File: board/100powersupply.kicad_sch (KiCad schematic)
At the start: 10 parts, among them J103 Conn_02x02_Counter_Clockwise, U101 TLS850C2TEV33

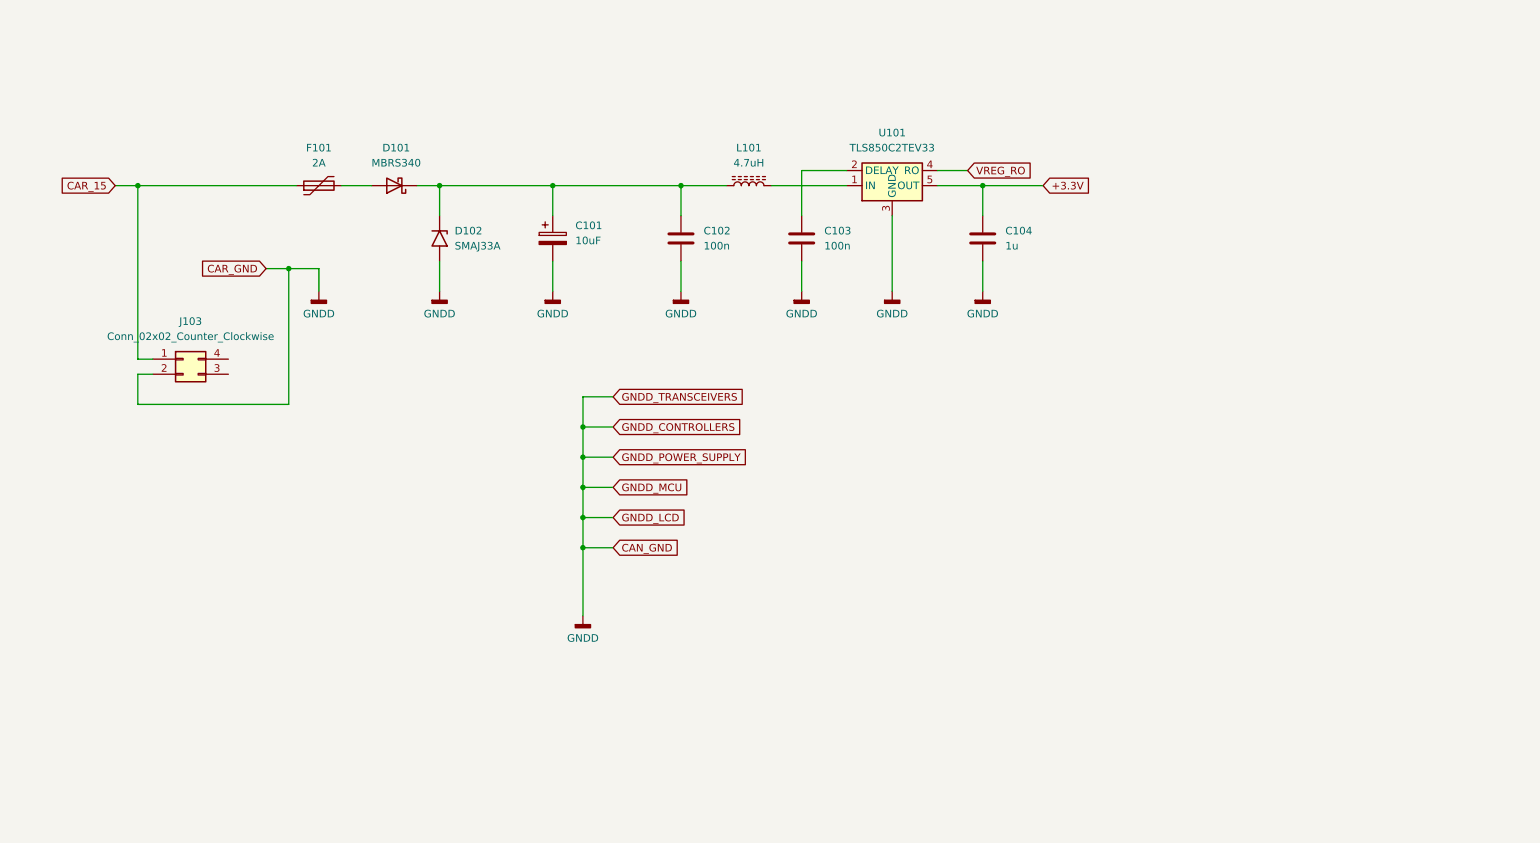
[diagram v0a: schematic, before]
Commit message: Added stl and skp files for 3D printing, changed ground planes and net names, exported schematics as pdf
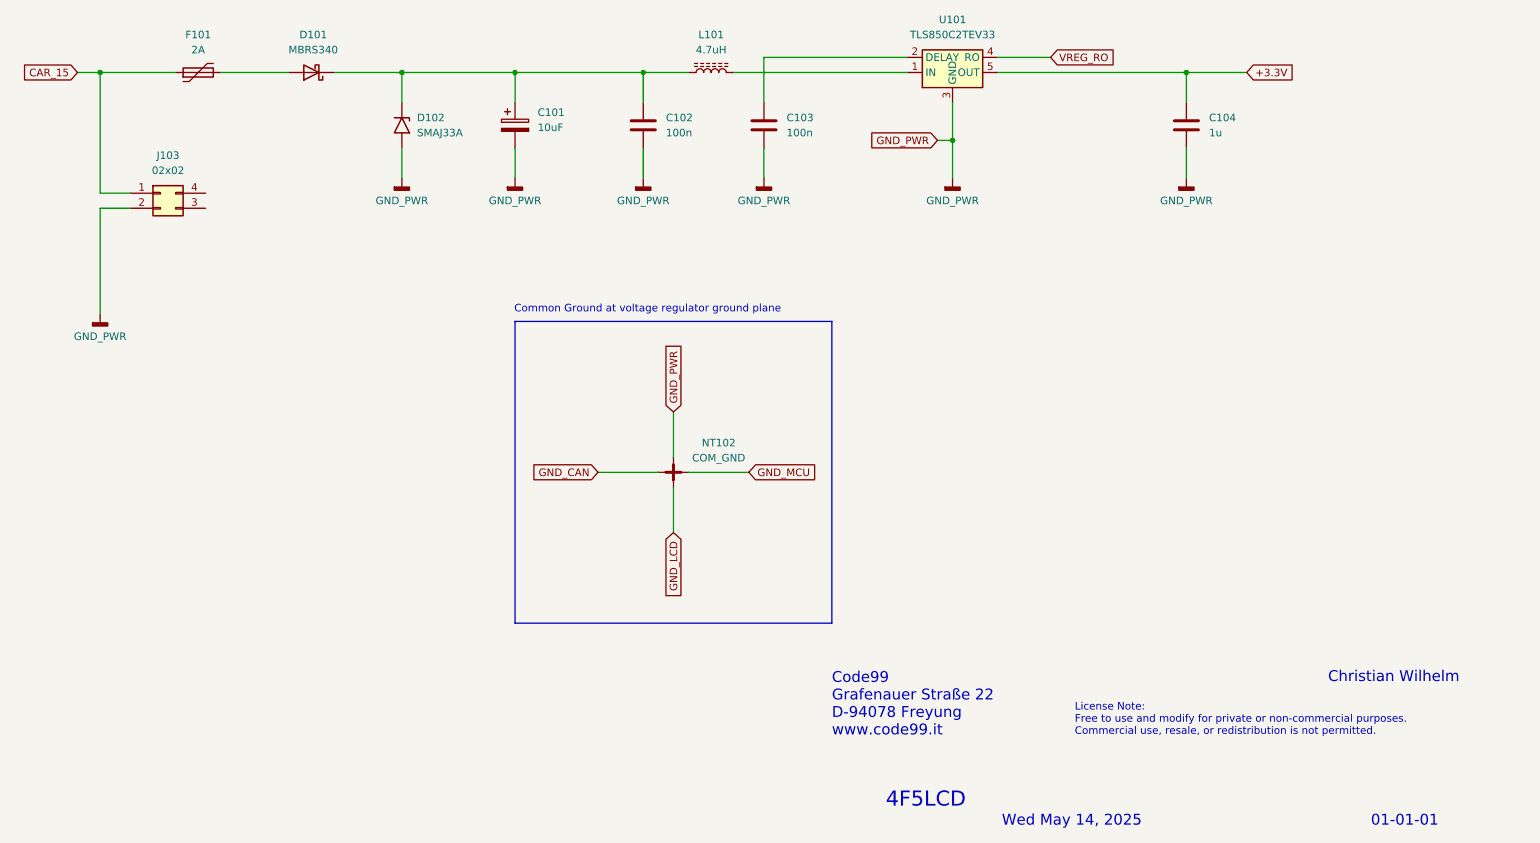
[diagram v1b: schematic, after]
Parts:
- added NT102: COM_GND, symbol Device:NetTie_4_Cross
- J103: value Conn_02x02_Counter_Clockwise -> 02x02
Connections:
- net GNDD renamed GND_PWR
- net GND_PWR: now also NT102.3
- new net GND_CAN: NT102.1
- new net GND_LCD: NT102.4
- new net GND_MCU: NT102.2
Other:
- note added: "01-01-01"
- note added: "4F5LCD"
- note added: "Christian Wilhelm"
- note added: "Code99 Grafenauer Straße 22 D-94078 Freyung www.code99.it"
- note added: "Common Ground at voltage regulator ground plane"
- note added: "License Note: Free to use and modify for private or non-commercial purposes. Commercial use, resale, or redistribution is not permitted."
- note added: "Wed May 14, 2025"
- moved on the sheet: C101, C102, C103, C104, D101, D102, F101, J103, L101, U101
